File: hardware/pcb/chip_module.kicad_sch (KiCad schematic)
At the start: 45 parts, among them J1 Samtec LSHM-130, Q1 AO3401A, Q10 AO3400A, Q11 AO3400A, Q12 AO3400A, Q13 AO3400A, Q14 AO3400A, Q15 AO3400A, Q16 AO3400A, Q2 AO3401A, Q3 AO3401A, Q4 AO3401A, Q5 AO3401A, Q6 AO3401A, Q7 AO3401A, Q8 AO3401A, Q9 AO3400A, U1 ADG732BCPZ, U2 ADG732BCPZ, U3 ADA4530-1, U4 74LVC1G04, U5 QSSC_Chip, U6 74HCT240, U7 74HCT240

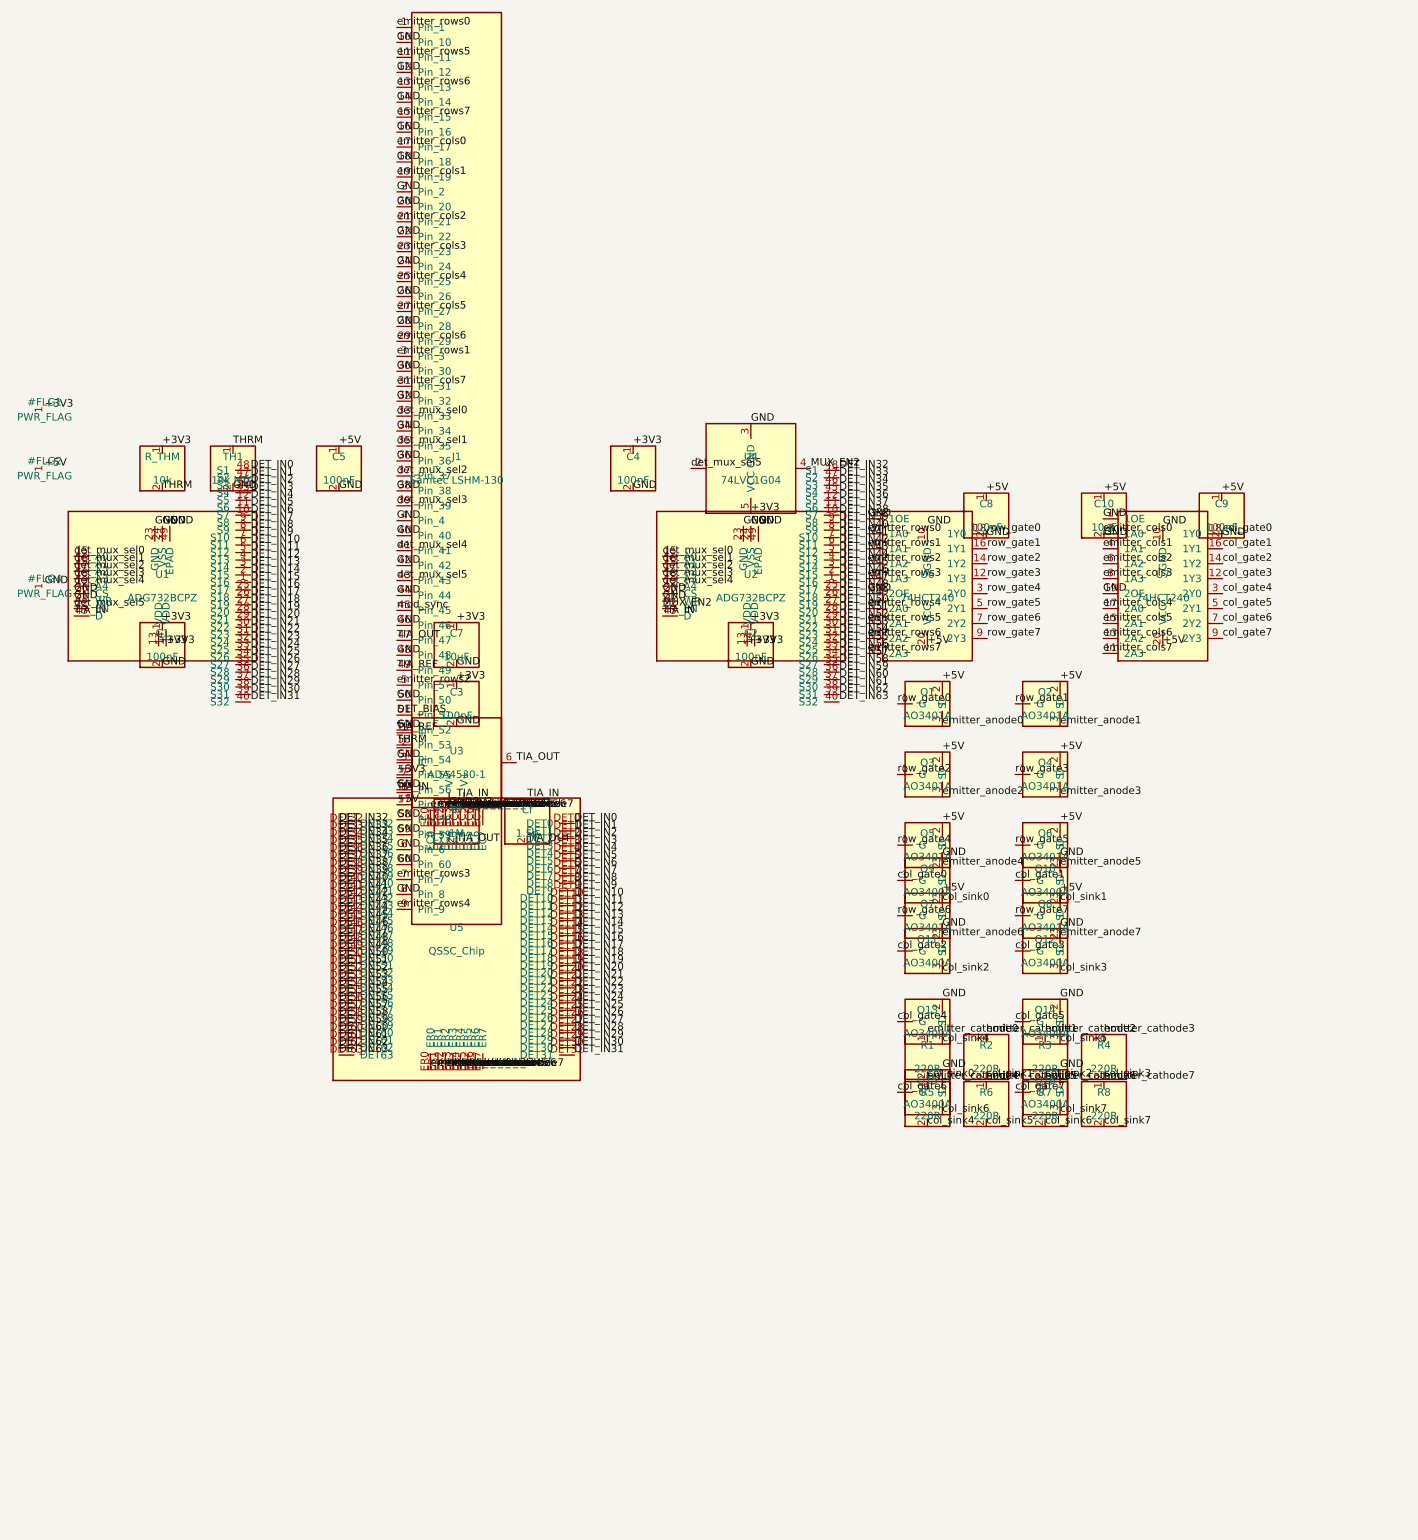
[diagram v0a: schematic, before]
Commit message: pcb: fix router keepout bugs -> both boards DRC-clean (0/0/0)
The headless line router had three keepout bugs that let a via or track
claim a cell another net already owned, producing DRC shorts on the
production-hardened (denser) board:

1. Centre-only via check. _via_candidates / _bga_edge_via_candidates /
   _via_point_clear only tested the via's centre cell per layer, but
   _add_via then marked a full r3 (0.6 mm) block on all four signal
   layers. A neighbour net's track 0.1-0.6 mm off-centre was invisible,
   so the via was placed and shorted it (CONF_DONE via vs CONF_INIT
   track on In4.Cu; TIA_ADC via vs VREFP track on B.Cu). Fixed with a
   _via_footprint_free helper that checks the full r3 footprint on all
   four signal layers before accepting any via-up.

2. multi_vip (BGA via-in-pad). The per-net vip_net "allowed" override
   seeded each ball's r2 mark on In3/In4/B.Cu. Adjacent 0.5 mm-pitch
   balls' r2 marks overlap by 0.3 mm, and the override let a net's own
   track/via-up enter that overlap -> ~0.10 mm clearance to the
   neighbour VIP. The multi_keepout fix (for pads) did not cover VIPs.
   Fixed by building a multi_vip set (cells in >=2 nets' VIP marks) and
   subtracting it from every net's vip_net, mirroring multi_keepout.

3. multi_keepout (pads) -- already applied last session (mw_gate->GND
   short on the D10 ESD diode). Kept; documented alongside multi_vip.

Result: both boards regenerate + route DRC-clean headlessly:
  qssc:        14/71 non-plane nets, 217 tracks, 95 vias, 0 DRC violations
  chip_module: 11/133 nets, 140 tracks, 47 vias, 0 DRC violations
ERC: 0 errors on both schematics (warnings only).

The router is now provably no-short-by-construction, but the correct
keepouts are conservative (a THROUGH via-up needs its full 0.6 mm
footprint clear on all four signal layers, which the dense 0.5 mm BGA
escape rarely affords), so completeness dropped from a buggy 37 (centre-
only check placed shorting vias) to a correct 14. The headles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
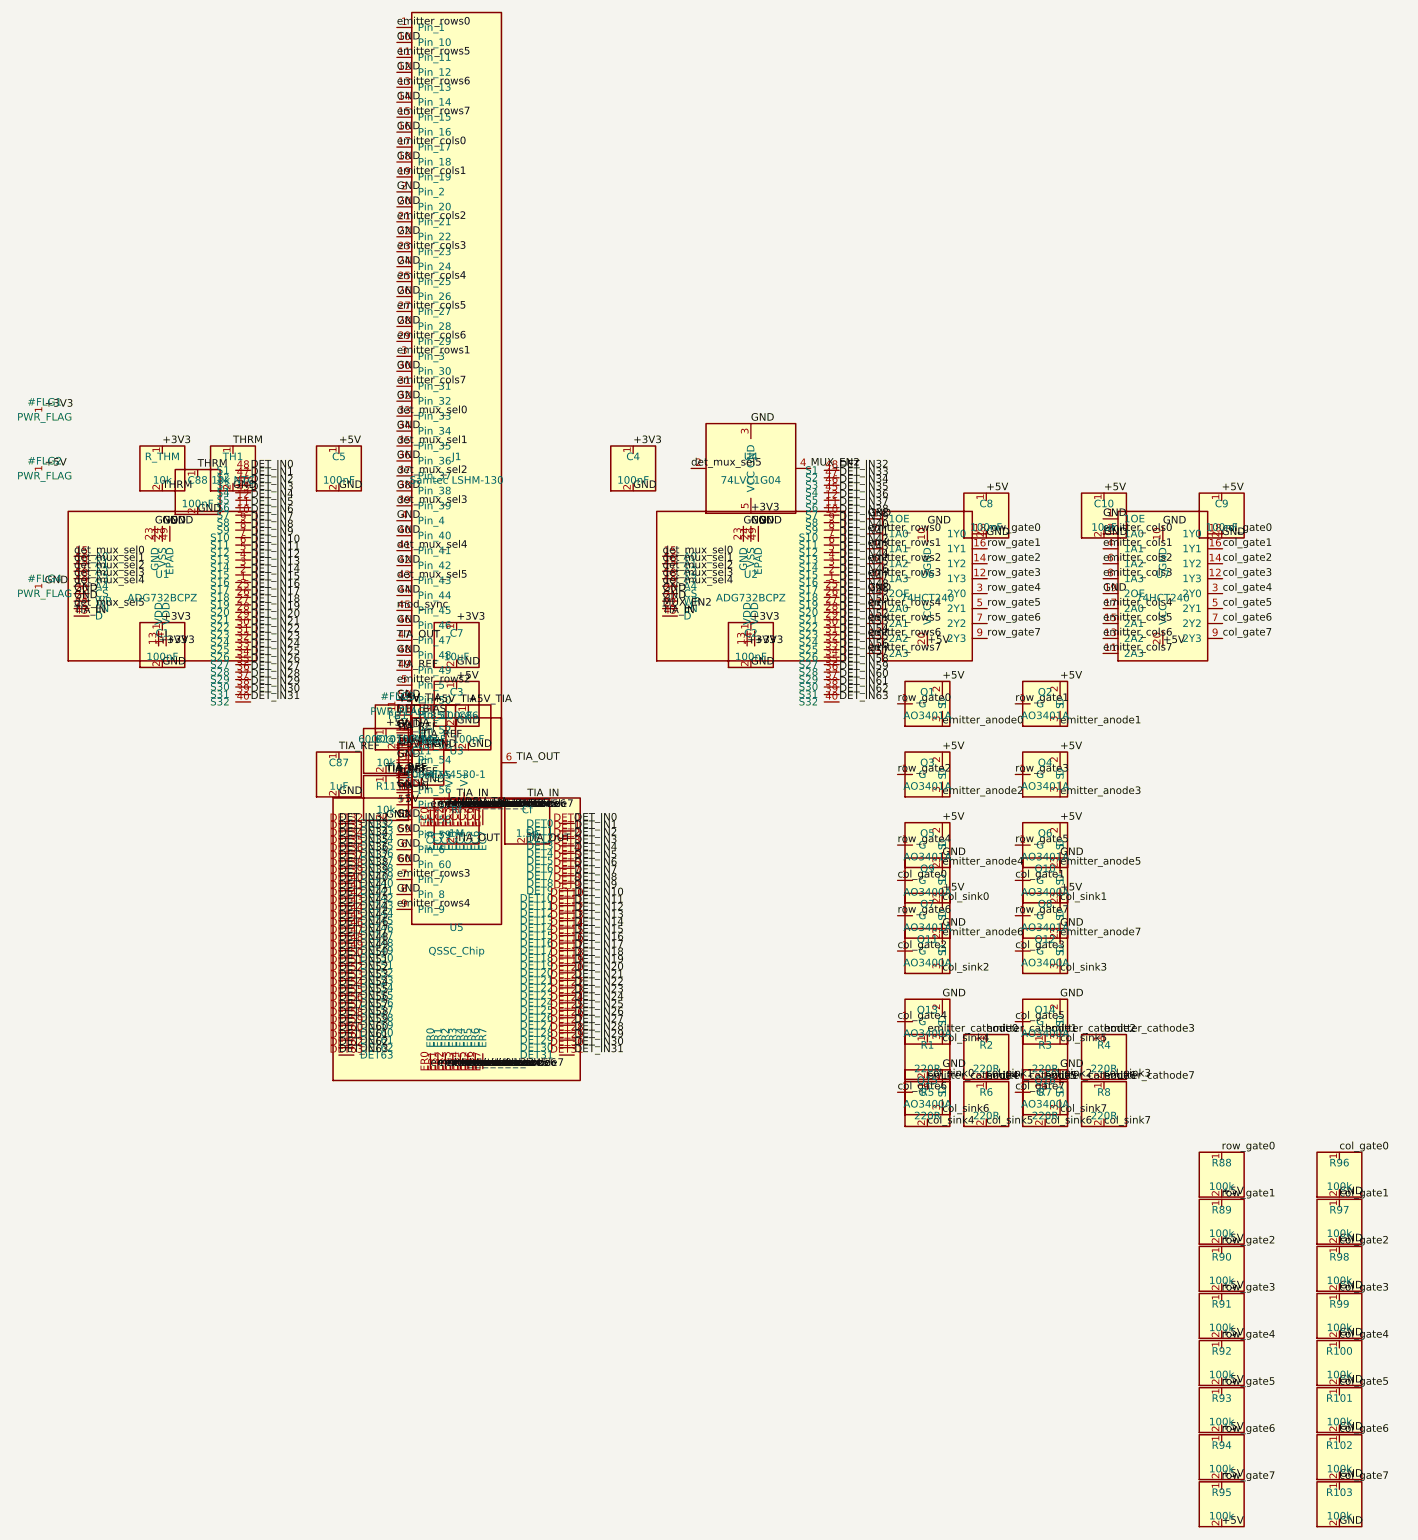
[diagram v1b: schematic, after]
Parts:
- added C11, C86, C88: 100nF, Capacitor_SMD:C_0603_1608Metric, symbol qssc:C
- added C85: 10uF, Capacitor_SMD:C_0805_2012Metric, symbol qssc:C
- added C87: 1uF, Capacitor_SMD:C_0603_1608Metric, symbol qssc:C
- added FB1: 600Ω@100MHz, Inductor_SMD:L_0603_1608Metric, symbol qssc:L
- added R10, R11: 10k, Resistor_SMD:R_0603_1608Metric, symbol qssc:R
- added R100, R101, R102, R103, R88, R89, R90, R91, R92, R93, R94, R95, R96, R97, R98, R99: 100k, Resistor_SMD:R_0603_1608Metric, symbol qssc:R
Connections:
- net +3V3: no longer C3.1, U3.5 (V+)
- net +5V: now also C3.1, FB1.1, R88.2, R89.2, R90.2, R91.2, R92.2, R93.2, R94.2, R95.2
- net GND: now also C11.2, C85.2, C86.2, C87.2, C88.2, R100.2, R101.2, R102.2, R103.2, R11.2, R96.2, R97.2, R98.2, R99.2
- net THRM: now also C88.1
- net TIA_REF: now also U3.2, U3.7, C11.1, C87.1, R10.2, R11.1
- net col_gate0: now also R96.1
- net col_gate1: now also R97.1
- net col_gate2: now also R98.1
- net col_gate3: now also R99.1
- net col_gate4: now also R100.1
- net col_gate5: now also R101.1
- net col_gate6: now also R102.1
- net col_gate7: now also R103.1
- net row_gate0: now also R88.1
- net row_gate1: now also R89.1
- net row_gate2: now also R90.1
- net row_gate3: now also R91.1
- net row_gate4: now also R92.1
- net row_gate5: now also R93.1
- net row_gate6: now also R94.1
- net row_gate7: now also R95.1
- new net +5V_TIA: C85.1, C86.1, FB1.2, R10.1, U3.5 (V+)
